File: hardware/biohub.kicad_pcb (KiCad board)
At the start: 2 copper layers, 55 x 55 mm, 15 parts, among them J1 1050170001, J2 Conn_02x13_Odd_Even, U1 VAL**, U2 UJ_5, U3 UJ_5, U4 ADP3605, U5 FT220XS, U6 VAL**, U7 RI_16_1, U8 UJ_5

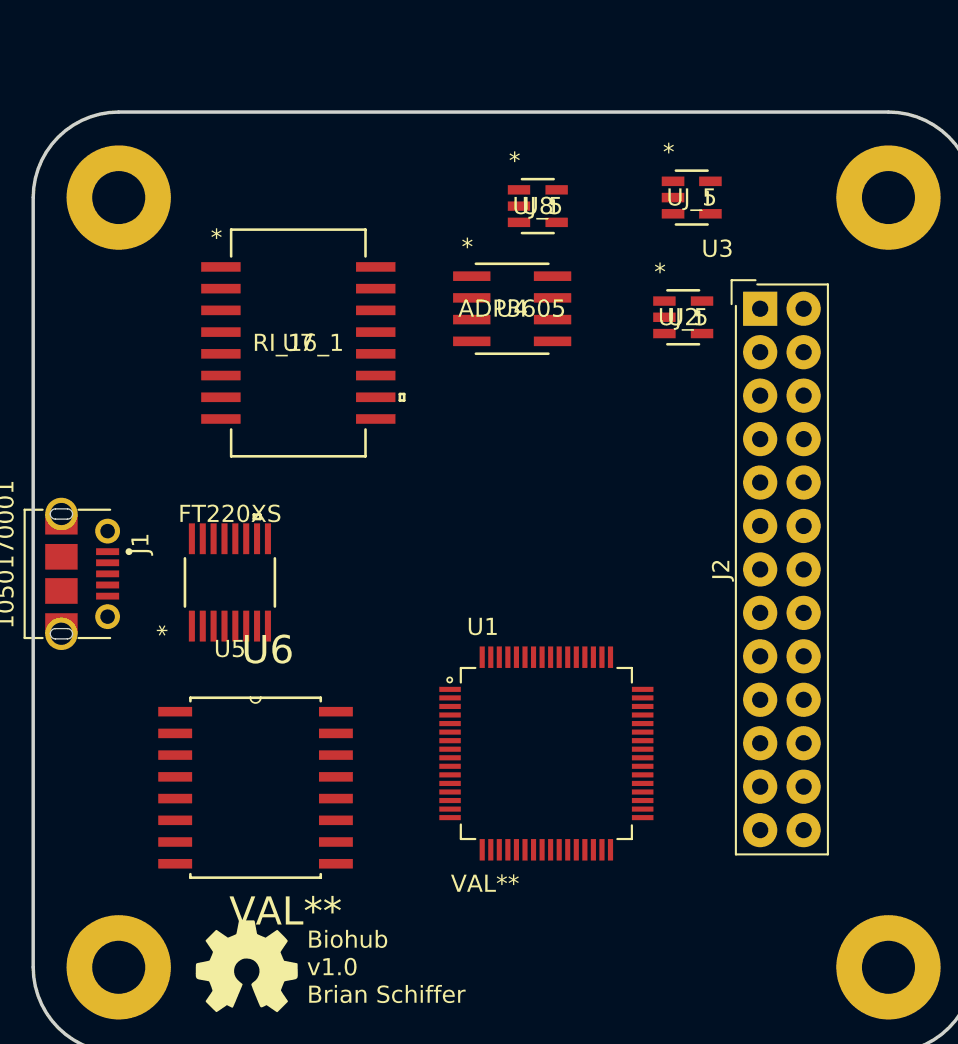
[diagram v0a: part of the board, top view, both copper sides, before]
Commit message: Added Buffers/ESD Protection
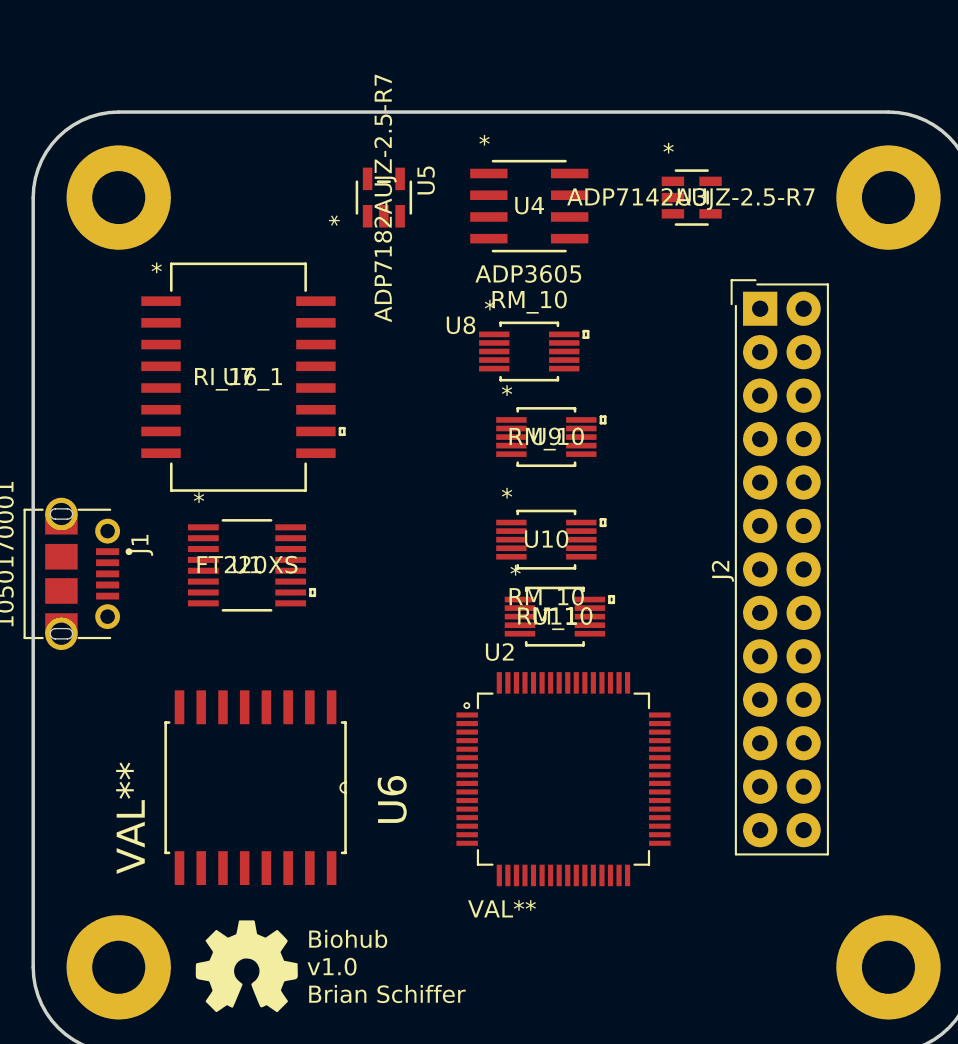
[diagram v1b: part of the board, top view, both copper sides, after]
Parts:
- added U10: RM_10, biohub:AD8244BRMZ, F.Cu at (240.0, 105.0)
- added U11: RM_10, biohub:AD8244BRMZ, F.Cu at (240.5, 109.5)
- added U9: RM_10, biohub:AD8244BRMZ, F.Cu at (240.0, 99.0)
- U1: value VAL** -> FT220XS; footprint biohub:ADS1299IPAG -> biohub:FT220X
- U2: value UJ_5 -> VAL**; footprint biohub:ADP7142AUJZ-R7 -> biohub:ADS1299IPAG
- U3: value UJ_5 -> ADP7142AUJZ-2.5-R7; footprint biohub:ADP7182AUJZ-R7 -> biohub:ADP7142AUJZ-R7
- U5: value FT220XS -> ADP7182AUJZ-2.5-R7; footprint biohub:FT220X -> biohub:ADP7182AUJZ-R7
- U8: value UJ_5 -> RM_10; footprint biohub:ADP7142AUJZ-R7 -> biohub:AD8244BRMZ
- moved U2 27.9 mm to (241.0, 119.0)
- moved U5 24.2 mm to (230.5, 85.0)
- moved U1 20.7 mm to (222.5, 106.5)
- moved U8 8.51 mm to (239.0, 94.0)
- moved U4 6.08 mm to (239.0, 85.5)
- moved U7 4.03 mm to (222.0, 95.5)
- turned U6 to 270 degrees
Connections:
- net Net-(U5-Pad5) renamed -2V5
- net Net-(U6-Pad11) renamed /MISO
- net Net-(U6-Pad12) renamed /CS
- net Net-(U6-Pad13) renamed /CLK
- net Net-(U6-Pad14) renamed /MOSI
- J1 pad 5: Net-(J1-Pad5) -> GNDD
- U1 pad 1: Net-(U1-Pad1) -> /USB_SPI_MOSI
- U1 pad 10: Net-(U1-Pad10) -> VCOM
- U1 pad 11: Net-(U1-Pad11) -> VCOM
- U1 pad 12: Net-(U1-Pad12) -> VBUS
- U1 pad 13: Net-(U1-Pad13) -> GNDD
- U1 pad 14: Net-(U1-Pad14) -> /USB_SPI_CS
- U1 pad 15: Net-(U1-Pad15) -> /USB_SPI_CLK
- U1 pad 3: Net-(U1-Pad3) -> VCOM
- U1 pad 5: Net-(U1-Pad5) -> GNDD
- U1 pad 7: Net-(U1-Pad7) -> /USB_SPI_MISO
- U3 pad 1: Net-(U3-Pad1) -> +3V3
- U3 pad 2: Net-(U3-Pad2) -> GND
- U3 pad 3: Net-(U3-Pad3) -> +3V3
- U3 pad 4: Net-(U3-Pad4) -> +2V5
- U3 pad 5: Net-(U3-Pad5) -> +2V5
- U4 pad 2: Net-(U4-Pad2) -> GND
- U4 pad 4: Net-(U4-Pad4) -> GND
- U4 pad 7: Net-(U4-Pad7) -> -3V3
- U4 pad 8: Net-(U4-Pad8) -> +3V3
- U5 pad 1: Net-(U5-Pad1) -> GND
- U5 pad 2: Net-(U5-Pad2) -> -3V3
- U5 pad 3: Net-(U5-Pad3) -> -3V3
- U6 pad 1: Net-(U6-Pad1) -> VCOM
- U6 pad 15: Net-(U6-Pad15) -> GND
- U6 pad 16: Net-(U6-Pad16) -> +3V3
- U6 pad 2: Net-(U6-Pad2) -> GNDD
- U6 pad 3: Net-(U6-Pad3) -> /USB_SPI_MOSI
- U6 pad 4: Net-(U6-Pad4) -> /USB_SPI_CLK
- U6 pad 5: Net-(U6-Pad5) -> /USB_SPI_CS
- U6 pad 6: Net-(U6-Pad6) -> /USB_SPI_MISO
- U6 pad 8: Net-(U6-Pad8) -> GNDD
- U6 pad 9: Net-(U6-Pad9) -> GND
- U7 pad 11: Net-(U7-Pad11) -> GND
- U7 pad 13: Net-(U7-Pad13) -> GND
- U7 pad 14: Net-(U7-Pad14) -> GND
- U7 pad 15: Net-(U7-Pad15) -> GND
- U7 pad 2: Net-(U7-Pad2) -> GNDD
- U7 pad 3: Net-(U7-Pad3) -> GNDD
- U7 pad 4: Net-(U7-Pad4) -> GNDD
- U7 pad 5: Net-(U7-Pad5) -> VBUS
- U7 pad 6: Net-(U7-Pad6) -> GNDD
- U7 pad 8: Net-(U7-Pad8) -> GNDD
- U7 pad 9: Net-(U7-Pad9) -> GND

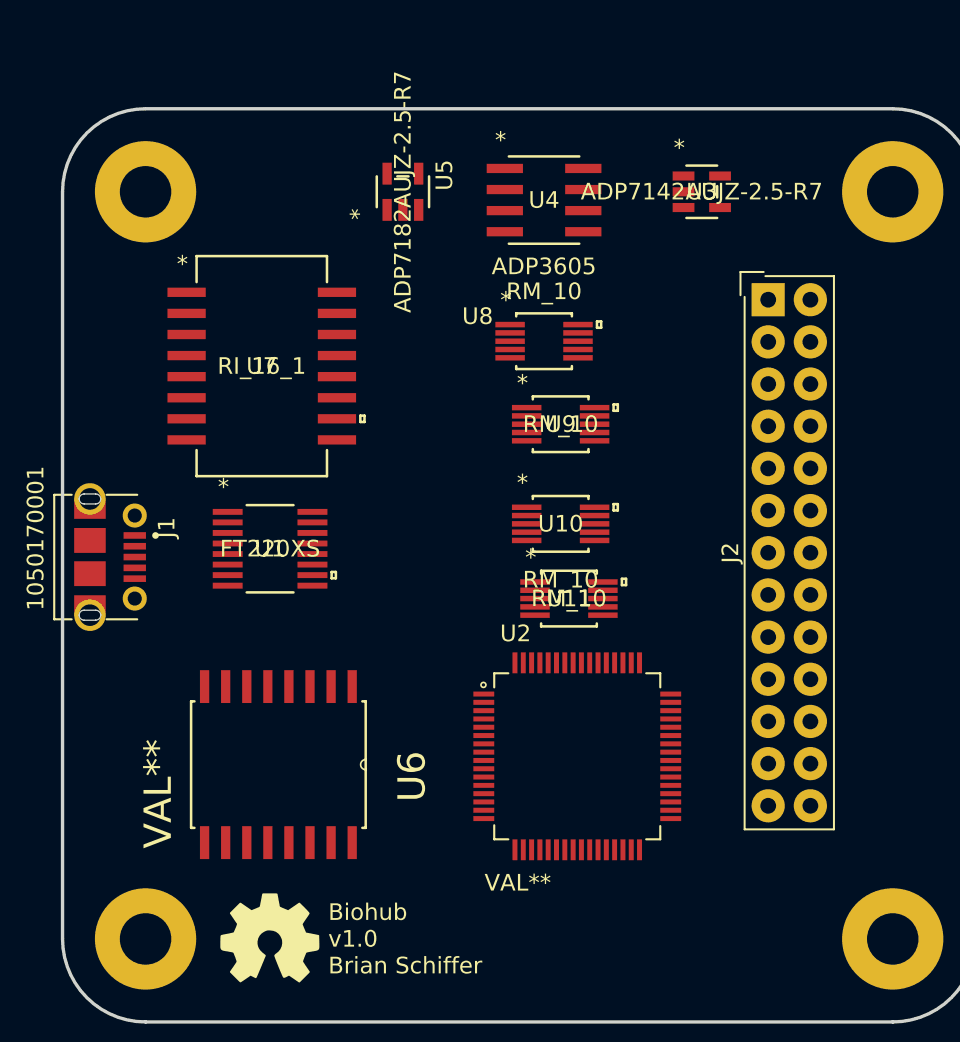
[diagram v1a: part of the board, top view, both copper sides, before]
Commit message: Updated to heirarchy sheets
Also added more ESD protection
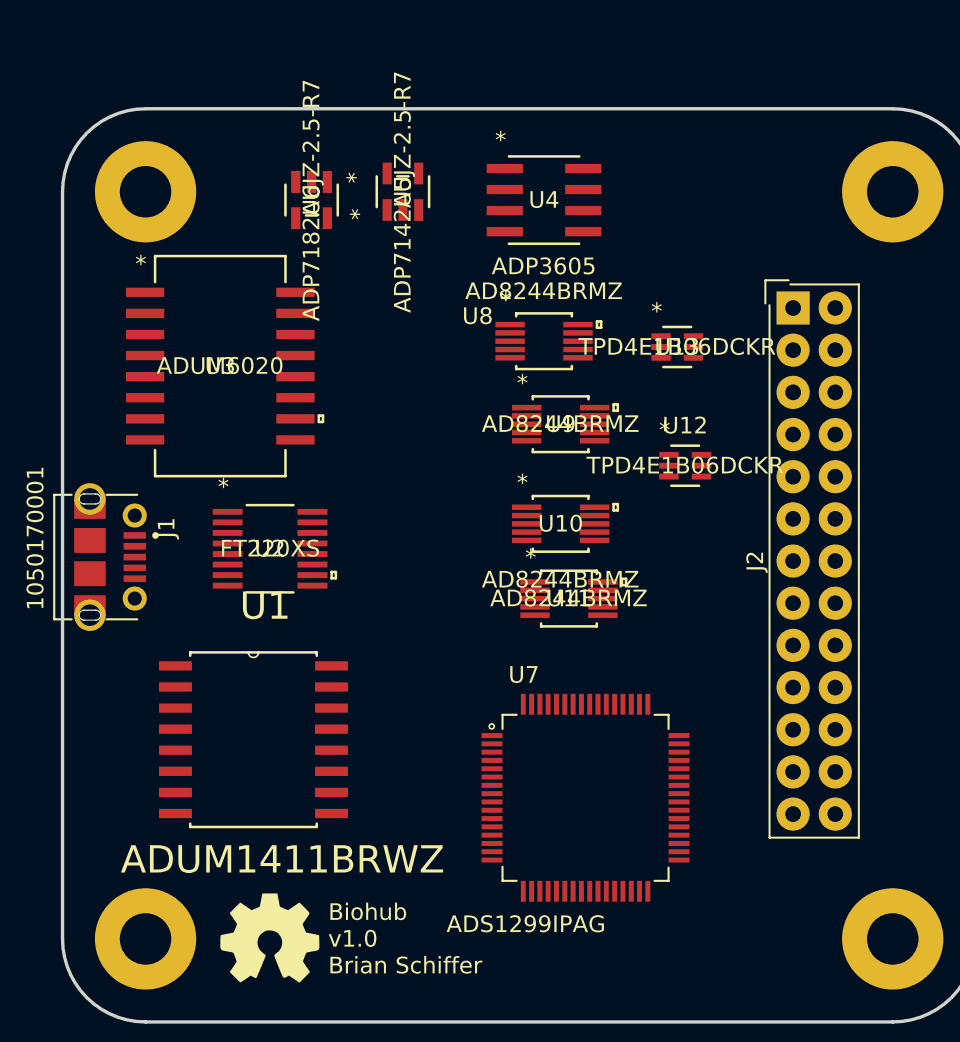
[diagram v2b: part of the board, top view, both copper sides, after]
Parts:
- added U12: TPD4E1B06DCKR, TPD4E1B06DCKR, F.Cu at (247.5, 101.5)
- added U13: TPD4E1B06DCKR, TPD4E1B06DCKR, F.Cu at (247.0, 94.4)
- U1: value FT220XS -> ADUM1411BRWZ; footprint biohub:FT220X -> biohub:ADUM1411BRWZ
- U10, U11, U8, U9: value RM_10 -> AD8244BRMZ
- U2: value VAL** -> FT220XS; footprint biohub:ADS1299IPAG -> biohub:FT220X
- U3: value ADP7142AUJZ-2.5-R7 -> ADUM6020; footprint biohub:ADP7142AUJZ-R7 -> biohub:ADUM6020
- U5: value ADP7182AUJZ-2.5-R7 -> ADP7142AUJZ-2.5-R7; footprint biohub:ADP7182AUJZ-R7 -> biohub:ADP7142AUJZ-R7
- U6: value VAL** -> ADP7182AUJZ-2.5-R7; footprint biohub:ADUM1411BRWZ -> biohub:ADP7182AUJZ-R7
- U7: value RI_16_1 -> ADS1299IPAG; footprint biohub:ADUM6020 -> biohub:ADS1299IPAG
- moved U6 34.1 mm to (225.0, 85.5)
- moved U7 32.5 mm to (241.5, 121.5)
- moved U3 30.8 mm to (219.5, 95.5)
- moved U2 22.3 mm to (222.5, 106.5)
- moved U1 11.5 mm to (221.5, 118.0)
- moved J2 1.58 mm to (254.0, 92.0)
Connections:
- net Net-(J2-Pad10) renamed /interface/7P
- net Net-(J2-Pad11) renamed /interface/6N
- net Net-(J2-Pad12) renamed /interface/6P
- net Net-(J2-Pad13) renamed /interface/5N
- net Net-(J2-Pad14) renamed /interface/5P
- net Net-(J2-Pad15) renamed /interface/4N
- net Net-(J2-Pad16) renamed /interface/4P
- net Net-(J2-Pad17) renamed /interface/3N
- net Net-(J2-Pad18) renamed /interface/3P
- net Net-(J2-Pad19) renamed /interface/2N
- net Net-(J2-Pad20) renamed /interface/2P
- net Net-(J2-Pad21) renamed /interface/1N
- net Net-(J2-Pad22) renamed /interface/1P
- net Net-(J2-Pad7) renamed /interface/8N
- net Net-(J2-Pad8) renamed /interface/8P
- net Net-(J2-Pad9) renamed /interface/7N
- net Net-(U7-Pad1) renamed /AFE/IN8N
- net Net-(U7-Pad10) renamed /AFE/IN4P
- net Net-(U7-Pad16) renamed /AFE/IN1P
- net Net-(U7-Pad7) renamed /AFE/IN5N
- J2 pad 1: Net-(J2-Pad1) -> +2V5
- J2 pad 2: Net-(J2-Pad2) -> +2V5
- J2 pad 23: Net-(J2-Pad23) -> /interface/SRB2
- J2 pad 24: Net-(J2-Pad24) -> /interface/SRB1
- J2 pad 25: Net-(J2-Pad25) -> -2V5
- J2 pad 26: Net-(J2-Pad26) -> -2V5
- J2 pad 3: Net-(J2-Pad3) -> GND
- J2 pad 4: Net-(J2-Pad4) -> GND
- J2 pad 5: Net-(J2-Pad5) -> /interface/BIAS
- J2 pad 6: Net-(J2-Pad6) -> /interface/BIAS
- U1 pad 1: /USB_SPI_MOSI -> VCOM
- U1 pad 10: VCOM -> Net-(U1-Pad10)
- U1 pad 11: VCOM -> /usb/MISO
- U1 pad 12: VBUS -> /usb/CS
- U1 pad 13: GNDD -> /usb/SCLK
- U1 pad 14: /USB_SPI_CS -> /usb/MOSI
- U1 pad 15: /USB_SPI_CLK -> GND
- U1 pad 16: Net-(U1-Pad16) -> +3V3
- U1 pad 2: Net-(U1-Pad2) -> GNDD
- U1 pad 3: VCOM -> /usb/USB_SPI_MOSI
- U1 pad 4: Net-(U1-Pad4) -> /usb/USB_SPI_CLK
- U1 pad 5: GNDD -> /usb/USB_SPI_CS
- U1 pad 6: Net-(U1-Pad6) -> /usb/USB_SPI_MISO
- U1 pad 7: /USB_SPI_MISO -> Net-(U1-Pad7)
- U1 pad 8: Net-(R3-Pad1) (its old number) -> GNDD
- U1 pad 9: Net-(R2-Pad1) (its old number) -> GND
- U10 pad 3: Net-(U10-Pad3) -> +2V5
- U10 pad 8: Net-(U10-Pad8) -> +2V5
- U11 pad 3: Net-(U11-Pad3) -> +2V5
- U11 pad 8: Net-(U11-Pad8) -> +2V5
- U2 pad 1: Net-(U2-Pad1) -> /usb/USB_SPI_MOSI
- U2 pad 10: Net-(U2-Pad10) -> VCOM
- U2 pad 11: Net-(U2-Pad11) -> VCOM
- U2 pad 12: Net-(U2-Pad12) -> VBUS
- U2 pad 13: Net-(U2-Pad13) -> GNDD
- U2 pad 14: Net-(U2-Pad14) -> /usb/USB_SPI_CS
- U2 pad 15: Net-(U2-Pad15) -> /usb/USB_SPI_CLK
- U2 pad 3: Net-(U2-Pad3) -> VCOM
- U2 pad 5: Net-(U2-Pad5) -> GNDD
- U2 pad 7: Net-(U2-Pad7) -> /usb/USB_SPI_MISO
- U3 pad 1: +3V3 -> Net-(U3-Pad1)
- U3 pad 2: GND -> GNDD
- U3 pad 3: +3V3 -> GNDD
- U3 pad 4: +2V5 -> GNDD
- U3 pad 5: +2V5 -> VBUS
- U5 pad 1: GND -> +3V3
- U5 pad 2: -3V3 -> GND
- U5 pad 3: -3V3 -> +3V3
- U5 pad 4: Net-(U5-Pad4) -> +2V5
- U5 pad 5: -2V5 -> +2V5
- U6 pad 1: VCOM -> GND
- U6 pad 2: GNDD -> -3V3
- U6 pad 3: /USB_SPI_MOSI -> -3V3
- U6 pad 4: /USB_SPI_CLK -> Net-(U6-Pad4)
- U6 pad 5: /USB_SPI_CS -> -2V5
- U7 pad 11: GND -> /AFE/IN3N
- U7 pad 12: Net-(C11-Pad1) -> /AFE/IN3P
- U7 pad 13: GND -> /AFE/IN2N
- U7 pad 14: GND -> /AFE/IN2P
- U7 pad 15: GND -> /AFE/IN1N
- U7 pad 2: GNDD -> /AFE/IN8P
- U7 pad 3: GNDD -> /AFE/IN7N
- U7 pad 4: GNDD -> /AFE/IN7P
- U7 pad 5: VBUS -> /AFE/IN6N
- U7 pad 6: GNDD -> /AFE/IN6P
- U7 pad 8: GNDD -> /AFE/IN5P
- U7 pad 9: GND -> /AFE/IN4N
- U8 pad 3: Net-(U8-Pad3) -> +2V5
- U8 pad 8: Net-(U8-Pad8) -> +2V5
- U9 pad 3: Net-(U9-Pad3) -> +2V5
- U9 pad 8: Net-(U9-Pad8) -> +2V5
